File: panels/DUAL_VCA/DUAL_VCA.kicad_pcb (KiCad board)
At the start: 2 copper layers, 70.8 x 128.4 mm, 13 parts

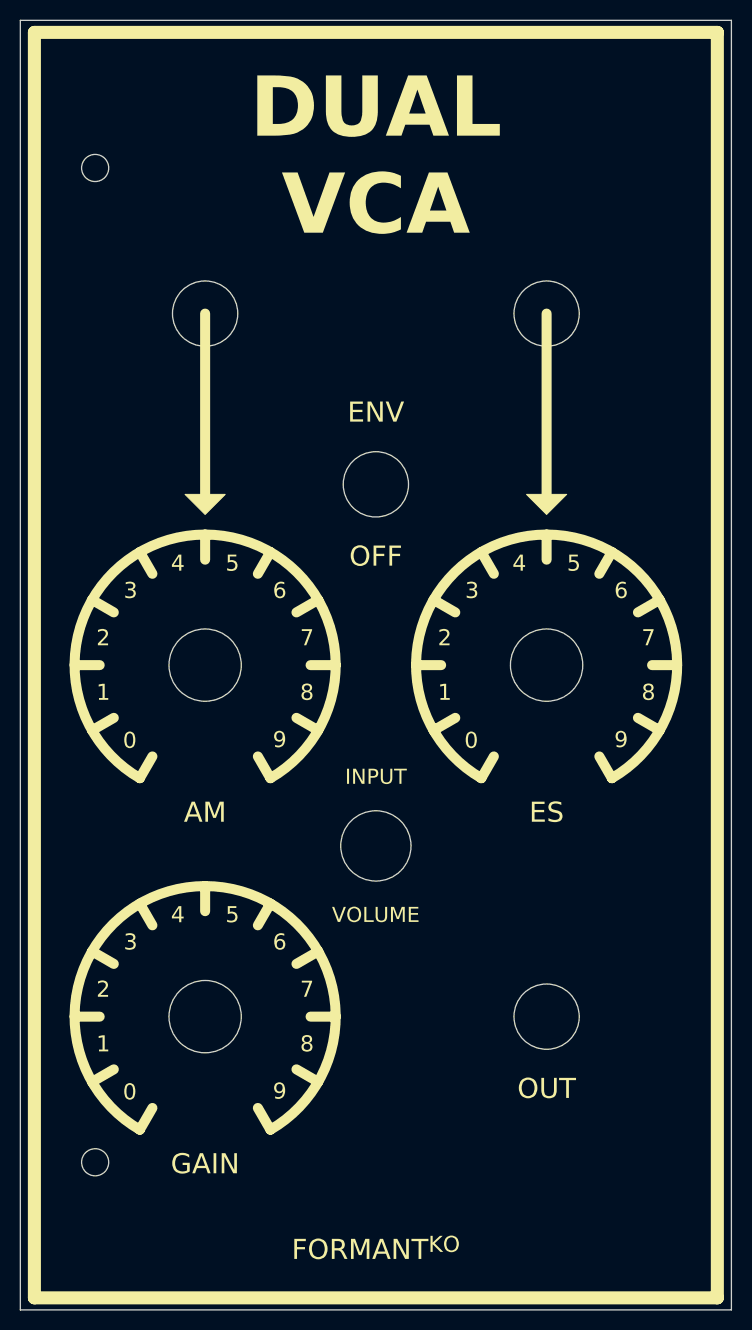
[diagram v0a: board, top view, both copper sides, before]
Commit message: updated adsr/dual vca
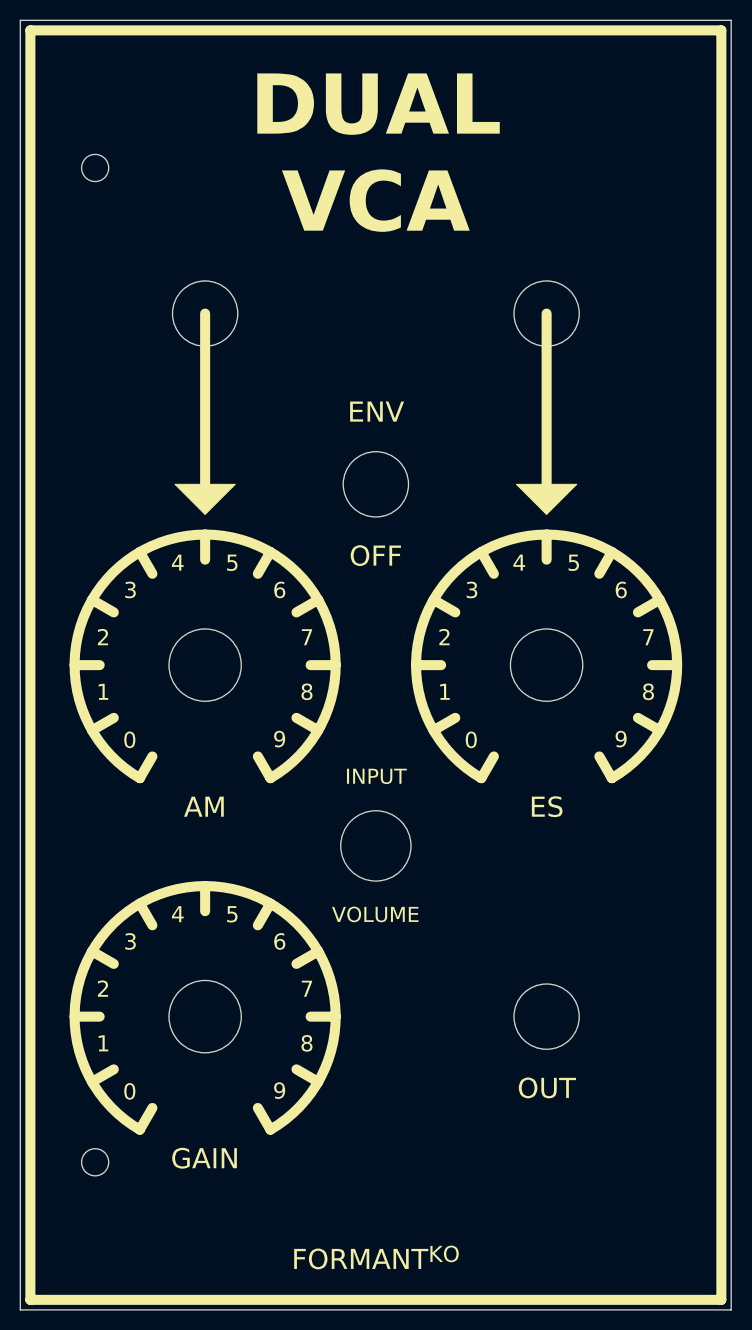
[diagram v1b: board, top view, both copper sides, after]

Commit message: panel templates, rfm
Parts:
- added REF**: Arrow, FormantKO-Panel:Arrow, F.Cu at (118.6, 89.7)
- added REF**: Arrow, FormantKO-Panel:Arrow, F.Cu at (84.6, 89.7)
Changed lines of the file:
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@@
 		)
+	)
+	(footprint "FormantKO-Panel:Arrow"
+		(layer "F.Cu")
+		(at 118.645894 89.715428)
+		(property "Reference" "REF**"
+			(at 0 -0.5 0)
+			(unlocked yes)
+			(layer "F.SilkS")
+			(hide yes)
+			(effects
+				(font
+					(size 1 1)
+					(thickness 0.1)
+				)
+			)
+		)
+		(property "Value" "Arrow"
+			(at 0 1 0)
+			(unlocked yes)
+			(layer "F.Fab")
+			(hide yes)
+			(effects
+				(font
+					(size 1 1)
+					(thickness 0.15)
+				)
+			)
+		)
+		(property "Datasheet" ""
+			(at 0 0 0)
+			(unlocked yes)
+			(layer "F.Fab")
+			(hide yes)
+			(effects
+				(font
+					(size 1 1)
+					(thickness 0.15)
+				)
+			)
+		)
+		(property "Description" ""
+			(at 0 0 0)
+			(unlocked yes)
+			(layer "F.Fab")
+			(hide yes)
+			(effects
+				(font
+					(size 1 1)
+					(thickness 0.15)
+				)
+			)
+		)
+		(attr smd)
+		(duplicate_pad_numbers_are_jumpers no)
+		(fp_poly
+			(pts
+				(xy 0 0) (xy -1.5 -2) (xy 1.5 -2)
+			)
+			(stroke
+				(width 0.1)
+				(type solid)
+			)
+			(fill yes)
+			(layer "F.SilkS")
+		)
+		(embedded_fonts no)
 	)
 	(footprint "FormantKO-Panel:PanelMountingHole"
@@
 		)
 	)
+	(footprint "FormantKO-Panel:Arrow"
+		(layer "F.Cu")
+		(at 84.645894 89.715428)
+		(property "Reference" "REF**"
+			(at 0 -0.5 0)
+			(unlocked yes)
+			(layer "F.SilkS")
+			(hide yes)
+			(effects
+				(font
+					(size 1 1)
+					(thickness 0.1)
+				)
+			)
+		)
+		(property "Value" "Arrow"
+			(at 0 1 0)
+			(unlocked yes)
+			(layer "F.Fab")
+			(hide yes)
+			(effects
+				(font
+					(size 1 1)
+					(thickness 0.15)
+				)
+			)
+		)
+		(property "Datasheet" ""
+			(at 0 0 0)
+			(unlocked yes)
+			(layer "F.Fab")
+			(hide yes)
+			(effects
+				(font
+					(size 1 1)
+					(thickness 0.15)
+				)
+			)
+		)
+		(property "Description" ""
+			(at 0 0 0)
+			(unlocked yes)
+			(layer "F.Fab")
+			(hide yes)
+			(effects
+				(font
+					(size 1 1)
+					(thickness 0.15)
+				)
+			)
+		)
+		(attr smd)
+		(duplicate_pad_numbers_are_jumpers no)
+		(fp_poly
+			(pts
+				(xy 0 0) (xy -1.5 -2) (xy 1.5 -2)
+			)
+			(stroke
+				(width 0.1)
+				(type solid)
+			)
+			(fill yes)
+			(layer "F.SilkS")
+		)
+		(embedded_fonts no)
+	)
 	(footprint "FormantKO-Panel:PanelMountingHole"
 		(layer "F.Cu")
@@
 		)
 	)
-	(gr_poly
-		(pts
-			(xy 84.645894 88.715428) (xy 81.645894 85.715428) (xy 87.645894 85.715428)
-		)
-		(stroke
-			(width 0.1)
-			(type solid)
-		)
-		(fill yes)
-		(layer "F.SilkS")
-	)
-	(gr_poly
-		(pts
-			(xy 118.645894 88.715428) (xy 115.645894 85.715428) (xy 121.645894 85.715428)
-		)
-		(stroke
-			(width 0.1)
-			(type solid)
-		)
-		(fill yes)
-		(layer "F.SilkS")
-	)
 	(gr_rect
